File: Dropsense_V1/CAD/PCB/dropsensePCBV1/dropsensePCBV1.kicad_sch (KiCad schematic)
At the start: 26 parts, among them J1 Micro_SD_Card_Det_Hirose_DM3AT, J2 USB_B_Micro, J3 Conn_01x02_Socket, SW1 SW_Push, SW2 SW_Push, U1 ESP32-S3-WROOM-1, U2 MPU-6050, U3 TP4056-42-ESOP8, U4 ME6211C10M5

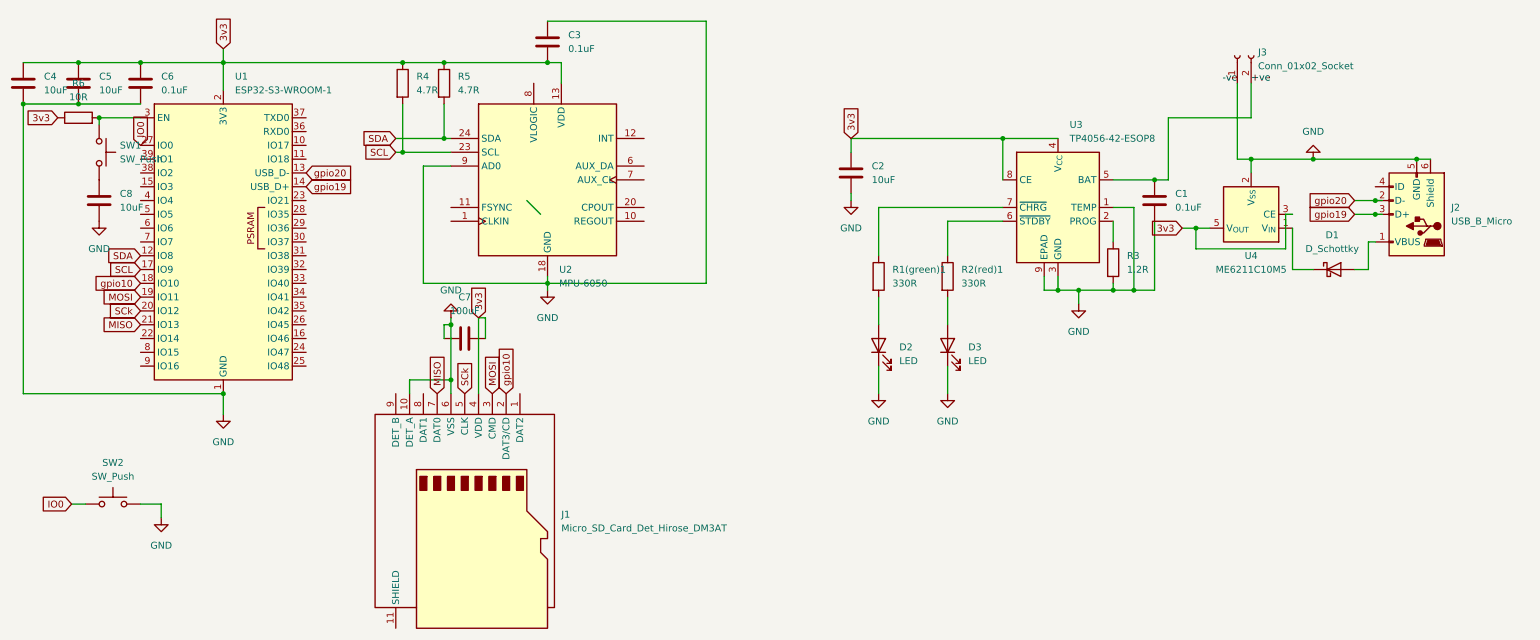
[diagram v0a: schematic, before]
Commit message: UPDATED DROPSENSE PCB
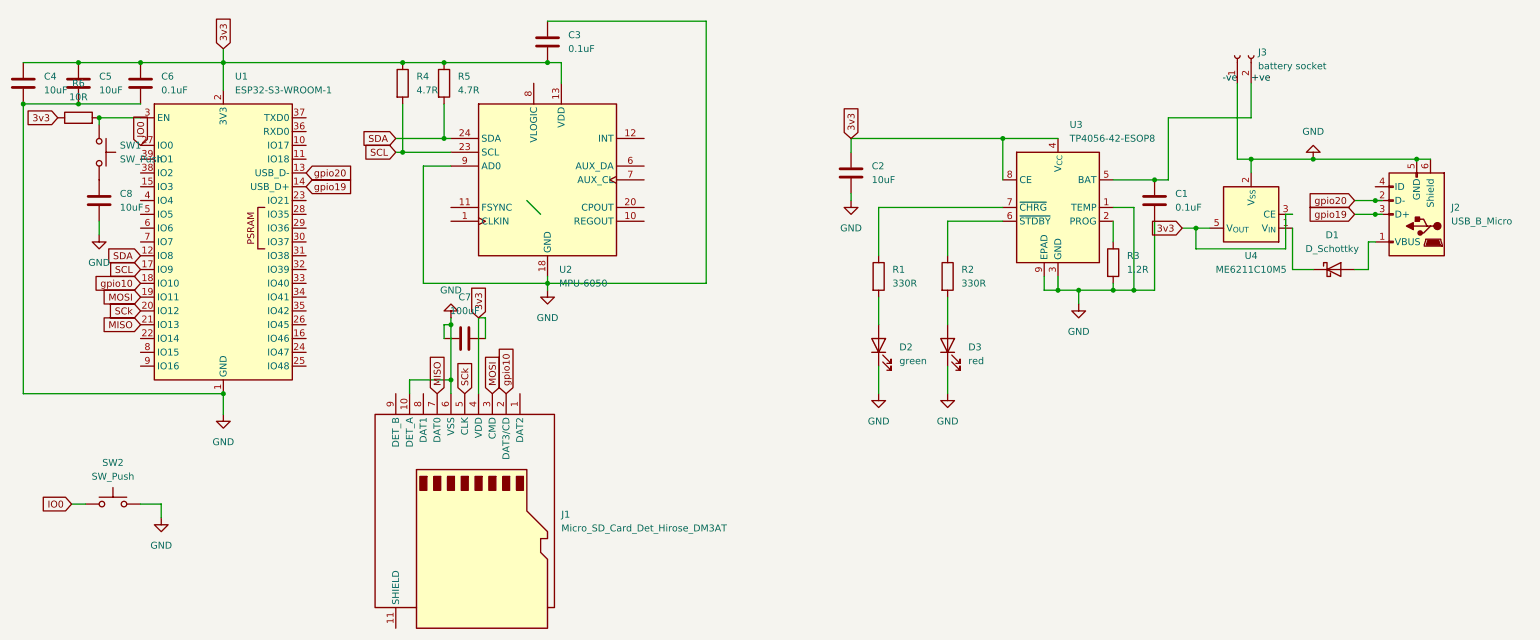
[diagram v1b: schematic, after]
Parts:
- D2: value LED -> green
- D3: value LED -> red
- J3: value Conn_01x02_Socket -> battery socket
- renumbered R1(green)1 to R1, R2(red)1 to R2
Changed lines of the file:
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@@
 	(wire
 		(pts
+			(xy 29.21 55.88) (xy 29.21 53.34)
+		)
+		(stroke
+			(width 0)
+			(type default)
+		)
+	)
+	(wire
+		(pts
 			(xy 167.64 38.1) (xy 195.58 38.1)
 		)
@@
 			)
 		)
-		(property "Value" "LED"
+		(property "Value" "red"
 			(at 189.23 79.0574 90)
 			(effects
@@
 		(dnp no)
 		(fields_autoplaced yes)
-		(property "Reference" "R2(red)1"
+		(property "Reference" "R2"
 			(at 187.96 62.2299 0)
 			(effects
@@
 			(project "dropsensePCBV1"
 				(path "/69b1a30b-982d-40a0-b848-7776f317f216"
-					(reference "R2(red)1")
+					(reference "R2")
 					(unit 1)
 				)
@@
 			)
 		)
-		(property "Value" "Conn_01x02_Socket"
+		(property "Value" "battery socket"
 			(at 242.57 24.7649 90)
 			(effects
@@
 		(dnp no)
 		(fields_autoplaced yes)
-		(property "Reference" "R1(green)1"
+		(property "Reference" "R1"
 			(at 175.26 62.2299 0)
 			(effects
@@
 			(project ""
 				(path "/69b1a30b-982d-40a0-b848-7776f317f216"
-					(reference "R1(green)1")
+					(reference "R1")
 					(unit 1)
 				)
@@
 	(symbol
 		(lib_id "power:GND")
-		(at 29.21 53.34 0)
+		(at 29.21 55.88 0)
 		(unit 1)
 		(exclude_from_sim no)
@@
 		(fields_autoplaced yes)
 		(property "Reference" "#PWR09"
-			(at 29.21 59.69 0)
+			(at 29.21 62.23 0)
 			(effects
 				(font
@@
 		)
 		(property "Value" "GND"
-			(at 29.21 58.42 0)
+			(at 29.21 60.96 0)
 			(effects
 				(font
@@
 		)
 		(property "Footprint" ""
-			(at 29.21 53.34 0)
+			(at 29.21 55.88 0)
 			(effects
 				(font
@@
 		)
 		(property "Datasheet" ""
-			(at 29.21 53.34 0)
+			(at 29.21 55.88 0)
 			(effects
 				(font
@@
 		)
 		(property "Description" "Power symbol creates a global label with name \"GND\" , ground"
-			(at 29.21 53.34 0)
+			(at 29.21 55.88 0)
 			(effects
 				(font
@@
 			)
 		)
-		(property "Value" "LED"
+		(property "Value" "green"
 			(at 176.53 79.0574 90)
 			(effects
